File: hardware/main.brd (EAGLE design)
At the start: 64.8 x 34 mm, 10 parts, among them U1 TXB0101_DBV_6, U2 SST25VF080BS2AF

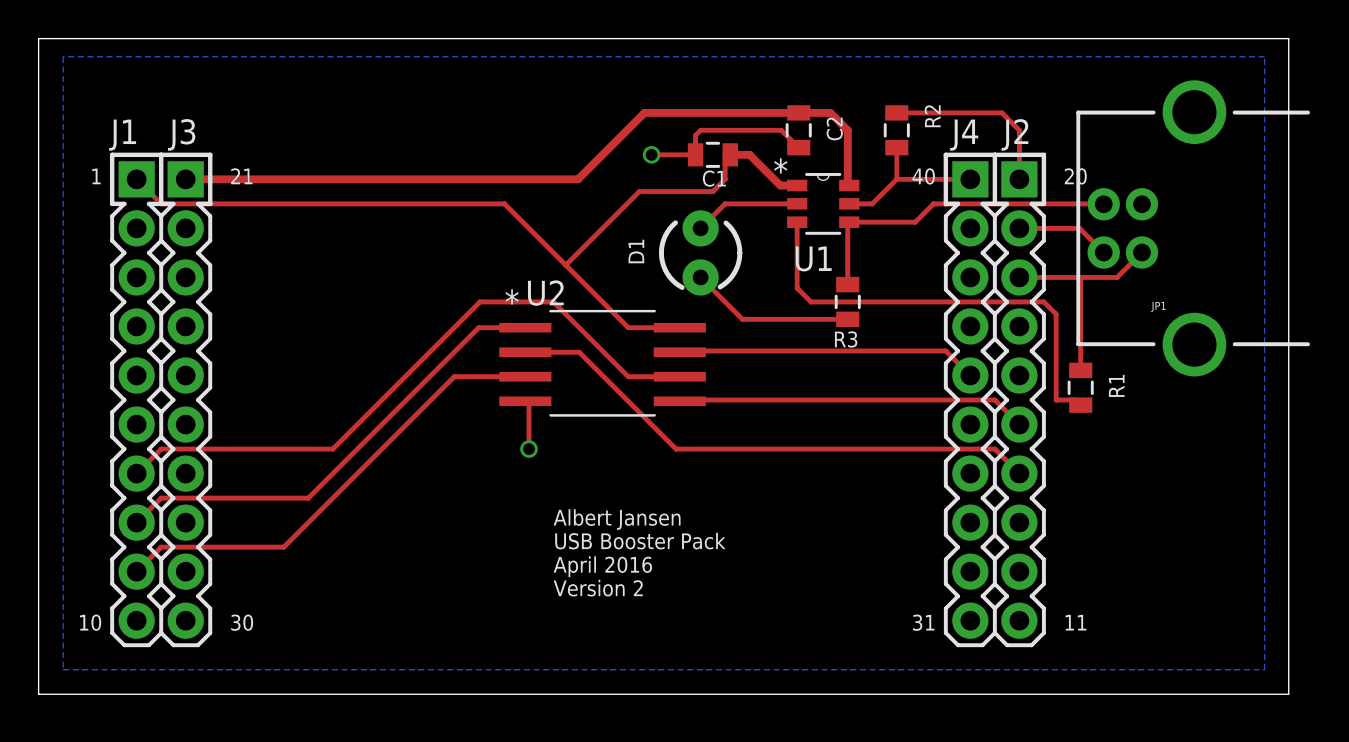
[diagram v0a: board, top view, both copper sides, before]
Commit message: Updated routing and USB power
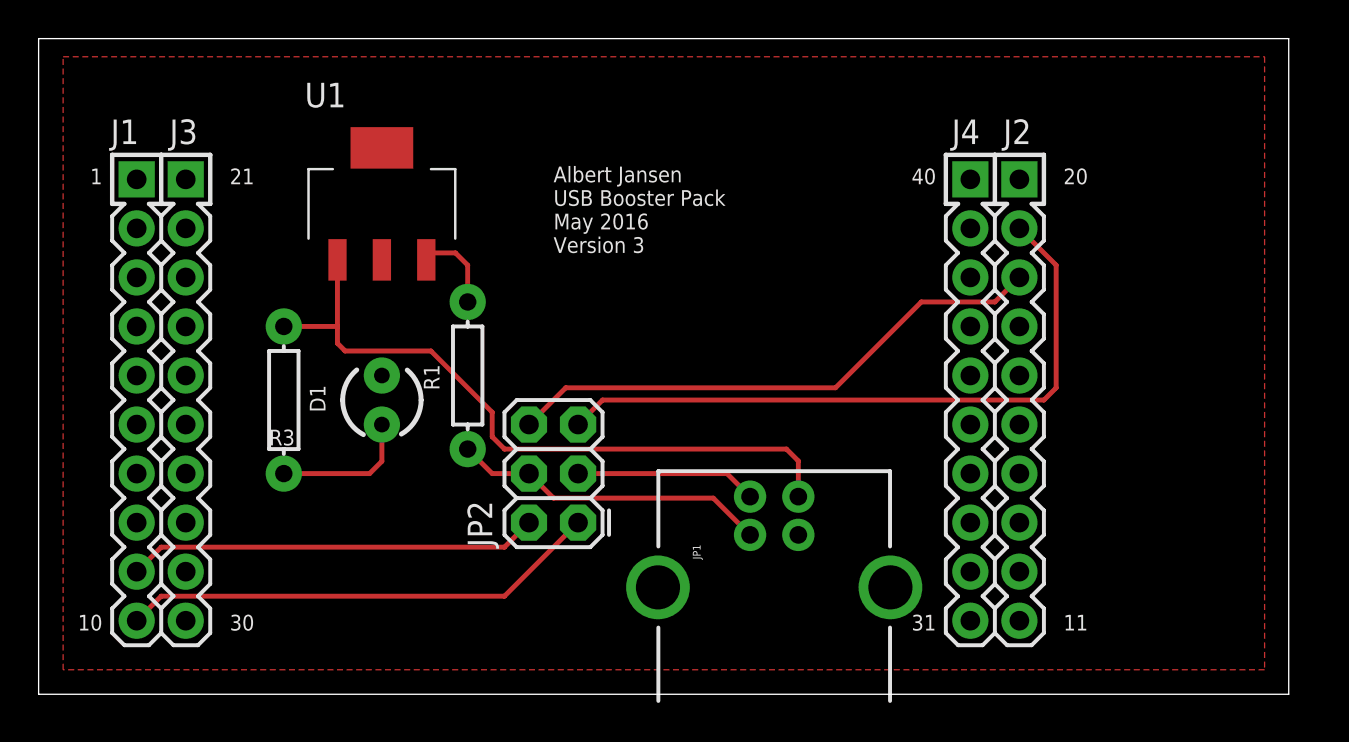
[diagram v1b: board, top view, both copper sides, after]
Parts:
- removed C1, C2: 0.1uF, SparkFun-Capacitors:0805
- removed R2: 10k, SparkFun-Resistors:0805
- removed U2: SST25VF080BS2AF, ControllerCard:S2AE/F
- added JP2: FEMALE 2x3, SparkFun-Connectors:2X3
- R1, R3: device SparkFun-Resistors:0805 -> SparkFun-Resistors:AXIAL-0.3
- U1: value TXB0101_DBV_6 -> LM3940SOT223; device ControllerCard:DBV6 -> ControllerCard:DCY
- moved R1 31.8 mm to (22.2, 16.5), turned to 90 degrees
- moved R3 29.6 mm to (12.7, 15.2)
- moved JP1 24.8 mm to (38.1, 8.26), turned to 90 degrees
- moved U1 22.9 mm to (17.8, 25.4)
- moved D1 18.2 mm to (17.8, 15.2)
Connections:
- removed net 5V: A1.21, C2.1, U1.6
- new net 377_N: A1.10, JP2.1
- new net 377_P: A1.9, JP2.2
- new net 69_N: A1.19, JP2.5
- new net 69_P: A1.18, JP2.6
- net !SPIEN!: no longer U2.P1
- net !SPIHOLD!: no longer U2.P7
- net !SPIWP!: now also A1.5; no longer A1.9, U2.P3
- net 3.3V: no longer C1.1, U1.1, U2.P8
- net ENEXT: no longer R2.2, U1.5
- net GND: now also U1.4; no longer C1.2, C2.2, R2.1, U2.P4
- net N$1: now also R3.P$1; no longer R3.1
- net SPICLK: no longer U2.P6
- net SPISIMO: no longer U2.P5
- net SPISOMI: no longer U2.P2
- net USBMON: now also R1.P$2; no longer R1.2
- net USB_N: now also JP2.3; no longer A1.19
- net USB_P: now also JP2.4, R1.P$1; no longer A1.18, R1.1
- net VBUS: now also R3.P$2, U1.1; no longer R3.2, U1.4
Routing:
- net 3.3V: track 47.4 -> 0.00 mm
- net 5V: track 39.0 -> 0.00 mm
- net 69_N: track 0.00 -> 34.6 mm
- net SPICLK: track 33.4 -> 0.00 mm
- net 69_P: track 0.00 -> 28.6 mm
- net SPISOMI: track 28.2 -> 0.00 mm
- net GND: track 26.5 -> 0.00 mm, vias 2 -> 0
- net 377_N: track 0.00 -> 25.0 mm
- net !SPIWP!: track 24.3 -> 0.00 mm
- net !SPIEN!: track 24.3 -> 0.00 mm
- net 377_P: track 0.00 -> 21.4 mm
- net VBUS: track 16.9 -> 36.1 mm
- net USBMON: track 23.2 -> 4.46 mm
- net SPISIMO: track 18.1 -> 0.00 mm
- net !SPIHOLD!: track 15.6 -> 0.00 mm
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- added copper zone on layer 1, net GND
- removed copper zone on layer 16, net GND
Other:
- board text added: "Albert Jansen USB Booster Pack May 2016 Version 3"
- board text removed: "Albert Jansen USB Booster Pack April 2016 Version 2"

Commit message: Finalized board against DRC, added aesthetics
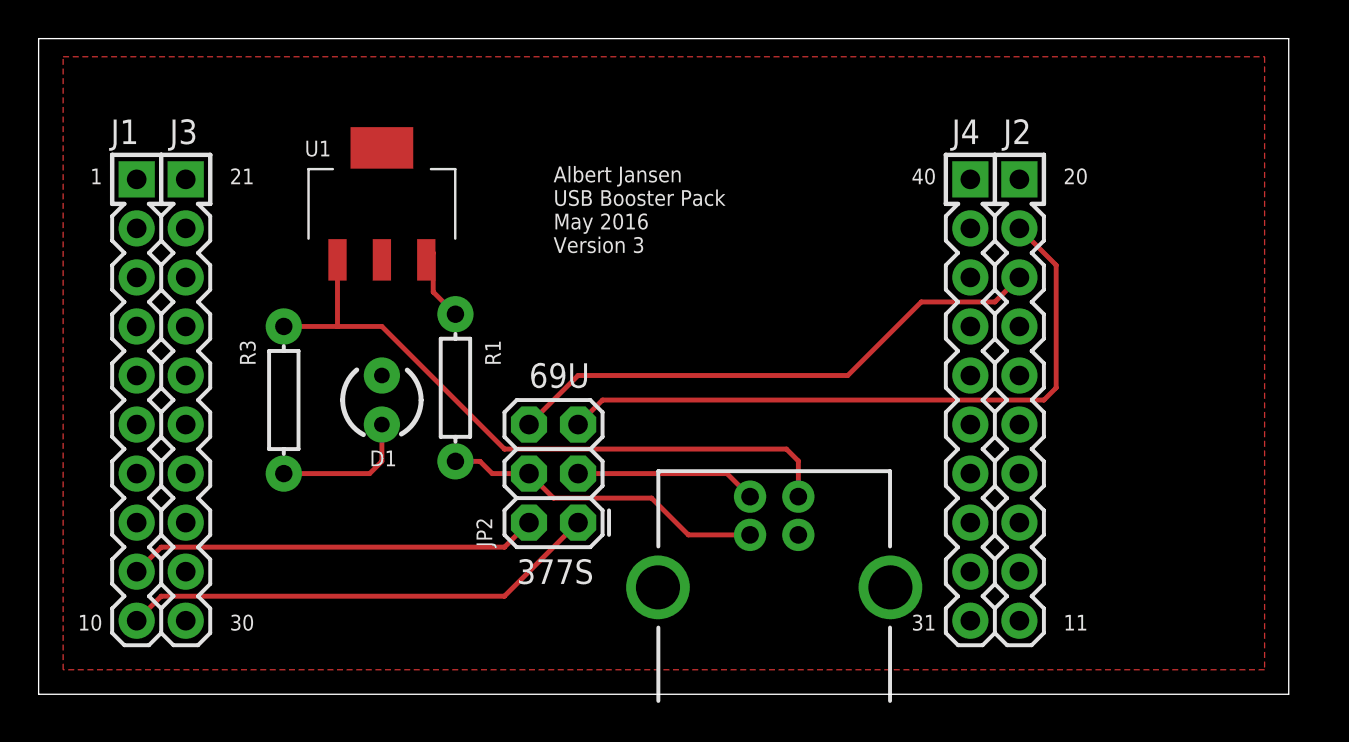
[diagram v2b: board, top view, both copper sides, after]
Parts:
- moved R1 0.90 mm to (21.6, 15.9)
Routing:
- net VBUS: track 36.1 -> 34.8 mm
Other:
- board text added: "377S"
- board text added: "69U"

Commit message: Minor update to component values. Added a BOM
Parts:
- R3: value 300 -> 330
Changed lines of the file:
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@@
 <attribute name="VALE" value="1k" x="21.59" y="15.875" size="1.778" layer="27" rot="R90" display="off"/>
 </element>
-<element name="R3" library="SparkFun-Resistors" package="AXIAL-0.3" value="300" x="12.7" y="15.24" smashed="yes" rot="R90">
+<element name="R3" library="SparkFun-Resistors" package="AXIAL-0.3" value="330" x="12.7" y="15.24" smashed="yes" rot="R90">
 <attribute name="PROD_ID" value="RES-08380" x="12.7" y="15.24" size="1.778" layer="27" rot="R90" display="off"/>
 <attribute name="NAME" x="11.2395" y="17.018" size="0.8128" layer="25" font="vector" rot="R90"/>
